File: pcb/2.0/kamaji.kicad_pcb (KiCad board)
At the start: 2 copper layers, 100 x 100 mm, 62 parts, among them J1 RJ10, J2 RJ10, J3 RJ10, J4 RJ10, J5 RJ10, J6 RJ10, J7 USB_B, J8 USB_A, Q1 2N3904, Q2 IRL540N, Q3 IRL540N, SW1 SW_Push, SW2 SW_Push, SW3 SW_Push, U1 ATMEGA32U4-AU, Y1 16MHz

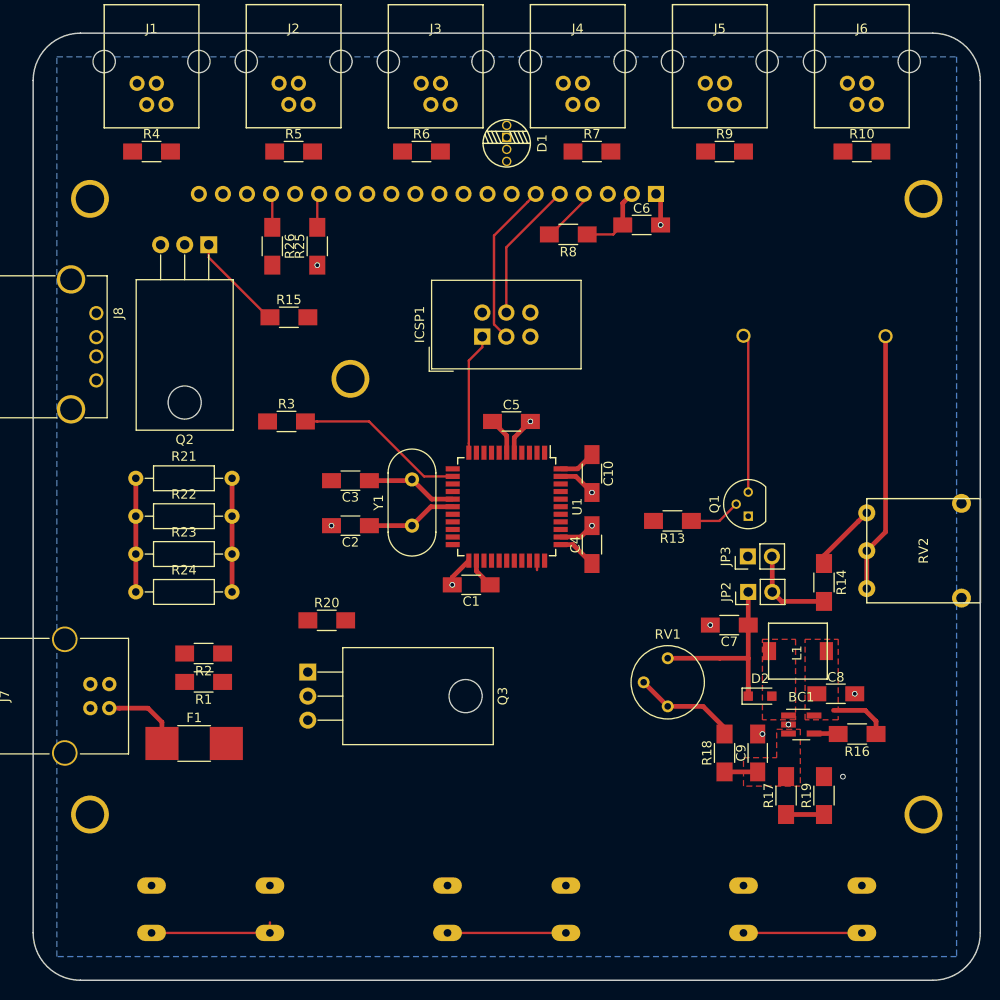
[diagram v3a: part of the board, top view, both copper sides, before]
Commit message: first attempt at laying out the 2.0 pcb
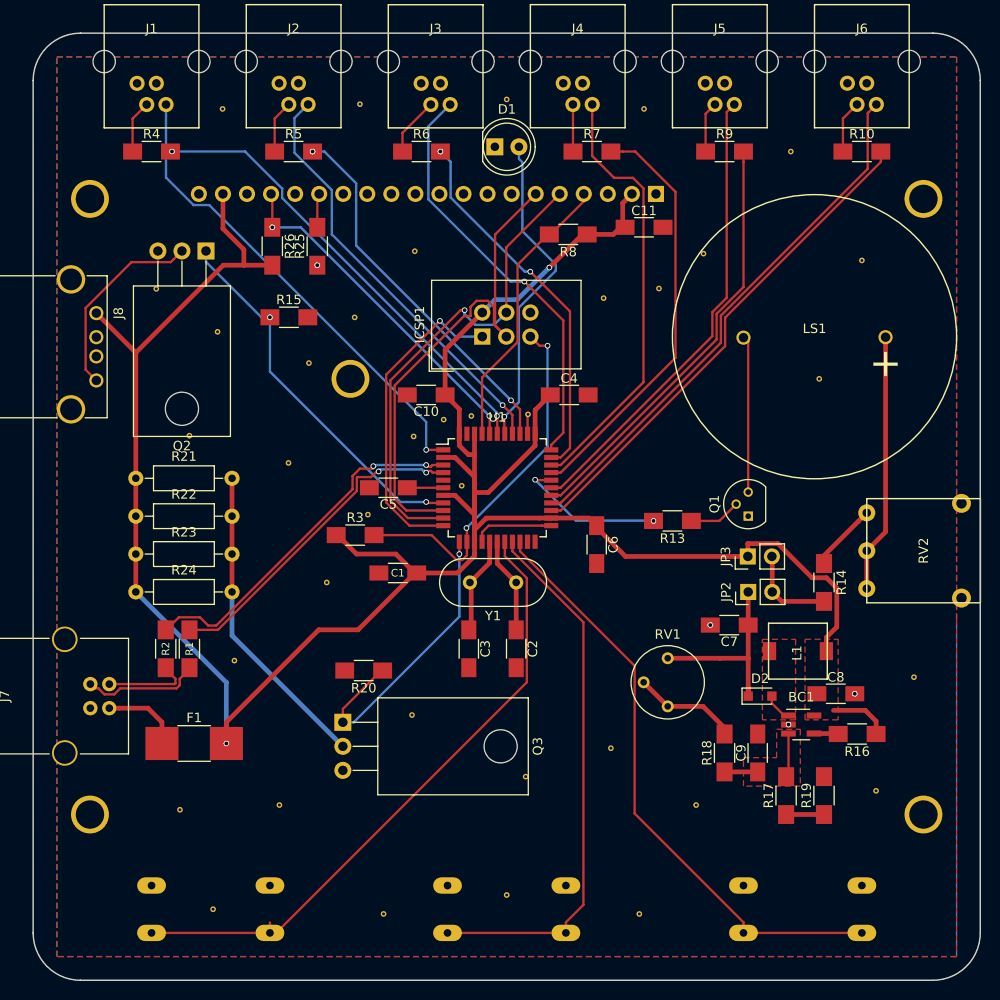
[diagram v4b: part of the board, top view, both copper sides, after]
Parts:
- added C11: 0.1uF, Capacitors_SMD:C_1206_HandSoldering, F.Cu at (114.5, 70.5)
- added REF**: Via_0.6mm, kamaji:Via_0.6mm, F.Cu at (102.2, 90.2)
- added REF**: Via_0.6mm, kamaji:Via_0.6mm, F.Cu at (71.2, 116.2)
- added REF**: Via_0.6mm, kamaji:Via_0.6mm, F.Cu at (81.0, 108.0)
- added REF**: Via_0.6mm, kamaji:Via_0.6mm, F.Cu at (90.0, 122.0)
- added REF**: Via_0.6mm, kamaji:Via_0.6mm, F.Cu at (65.5, 132.0)
- added REF**: Via_0.6mm, kamaji:Via_0.6mm, F.Cu at (69.0, 142.5)
- added REF**: Via_0.6mm, kamaji:Via_0.6mm, F.Cu at (76.0, 131.5)
- added REF**: Via_0.6mm, kamaji:Via_0.6mm, F.Cu at (87.0, 143.0)
- added REF**: Via_0.6mm, kamaji:Via_0.6mm, F.Cu at (100.0, 141.0)
- added REF**: Via_0.6mm, kamaji:Via_0.6mm, F.Cu at (102.0, 128.5)
- added REF**: Via_0.6mm, kamaji:Via_0.6mm, F.Cu at (111.0, 125.5)
- added REF**: Via_0.6mm, kamaji:Via_0.6mm, F.Cu at (63.0, 77.0)
- added REF**: Via_0.6mm, kamaji:Via_0.6mm, F.Cu at (114.0, 143.0)
- added REF**: Via_0.6mm, kamaji:Via_0.6mm, F.Cu at (120.0, 131.5)
- added REF**: Via_0.6mm, kamaji:Via_0.6mm, F.Cu at (143.0, 118.0)
- added REF**: Via_0.6mm, kamaji:Via_0.6mm, F.Cu at (139.0, 130.0)
- added REF**: Via_0.6mm, kamaji:Via_0.6mm, F.Cu at (120.8, 73.3)
- added REF**: Via_0.6mm, kamaji:Via_0.6mm, F.Cu at (116.1, 77.0)
- added REF**: Via_0.6mm, kamaji:Via_0.6mm, F.Cu at (110.2, 78.0)
- added REF**: Via_0.6mm, kamaji:Via_0.6mm, F.Cu at (90.3, 73.0)
- added REF**: Via_0.6mm, kamaji:Via_0.6mm, F.Cu at (83.9, 80.0)
- added REF**: Via_0.6mm, kamaji:Via_0.6mm, F.Cu at (79.1, 84.8)
- added REF**: Via_0.6mm, kamaji:Via_0.6mm, F.Cu at (70.0, 58.0)
- added REF**: Via_0.6mm, kamaji:Via_0.6mm, F.Cu at (69.5, 81.5)
- added REF**: Via_0.6mm, kamaji:Via_0.6mm, F.Cu at (66.5, 92.5)
- added REF**: Via_0.6mm, kamaji:Via_0.6mm, F.Cu at (77.0, 95.4)
- added REF**: Via_0.6mm, kamaji:Via_0.6mm, F.Cu at (85.3, 100.8)
- added REF**: Via_0.6mm, kamaji:Via_0.6mm, F.Cu at (90.2, 92.6)
- added REF**: Via_0.6mm, kamaji:Via_0.6mm, F.Cu at (93.3, 90.8)
- added REF**: Via_0.6mm, kamaji:Via_0.6mm, F.Cu at (96.3, 90.4)
- added REF**: Via_0.6mm, kamaji:Via_0.6mm, F.Cu at (95.2, 97.8)
- added REF**: Via_0.6mm, kamaji:Via_0.6mm, F.Cu at (84.5, 57.5)
- added REF**: Via_0.6mm, kamaji:Via_0.6mm, F.Cu at (100.0, 57.0)
- added REF**: Via_0.6mm, kamaji:Via_0.6mm, F.Cu at (114.5, 58.0)
- added REF**: Via_0.6mm, kamaji:Via_0.6mm, F.Cu at (130.0, 62.5)
- added REF**: Via_0.6mm, kamaji:Via_0.6mm, F.Cu at (137.5, 74.0)
- added REF**: Via_0.6mm, kamaji:Via_0.6mm, F.Cu at (133.0, 86.5)
- C1: value 0.1uF -> 10uF
- D1: value LED_CRGB -> LED; footprint kamaji:LED_RGB_common_cathode_5mm -> LEDs:LED_D5.0mm
- LS1: moved to F.Cu
- moved C6 34.1 mm to (109.5, 104.0), turned to 270 degrees
- moved C2 21.8 mm to (101.0, 115.0), turned to 270 degrees
- moved C3 21.7 mm to (96.0, 115.0), turned to 270 degrees
- moved C10 19.4 mm to (91.5, 88.2), turned to 180 degrees
- moved C4 16.0 mm to (106.6, 88.2), turned to 0 degrees
- moved C5 14.8 mm to (87.5, 98.0), turned to 180 degrees
- moved R3 14.0 mm to (84.0, 103.0)
- moved Y1 12.5 mm to (101.0, 108.0), turned to 180 degrees
- moved C1 7.85 mm to (88.5, 107.0)
- moved R20 6.58 mm to (84.9, 117.3), turned to 180 degrees
- moved Q3 6.46 mm to (82.7, 122.8)
- moved R2 4.03 mm to (64.0, 115.0), turned to 270 degrees
- moved R1 3.81 mm to (66.5, 115.0), turned to 270 degrees
- moved U1 2.24 mm to (99.0, 98.0), turned to 0 degrees
- moved D1 1.30 mm to (98.8, 62.0), turned to 0 degrees
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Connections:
- net /SIGNAL_R renamed /SIGNAL_LED
- J7 pad 2: /USB_D- -> /USBBD-
- J7 pad 3: /USB_D+ -> /USBBD+
- R1 pad 1: Net-(R1-Pad1) -> /USB_D+
- R1 pad 2: /USB_D+ -> /USBBD+
- R2 pad 1: Net-(R2-Pad1) -> /USB_D-
- R2 pad 2: /USB_D- -> /USBBD-
- U1 pad 1: /CBTN3 -> /PBTN1
- U1 pad 18: /PBTN1 -> /CBTN1
- U1 pad 19: /PLED1 -> /CBTN2
- U1 pad 20: /PBTN2 -> /CBTN3
- U1 pad 21: /PLED2 -> (no net)
- U1 pad 22: /PLED6 -> (no net)
- U1 pad 25: /PLED3 -> /PLED6
- U1 pad 26: /PBTN3 -> /PBTN6
- U1 pad 27: /PLED4 -> /PLED5
- U1 pad 28: /PBTN4 -> /PBTN5
- U1 pad 3: Net-(R2-Pad1) -> /USB_D-
- U1 pad 30: /PLED5 -> /PLED4
- U1 pad 31: /PBTN5 -> /PBTN4
- U1 pad 32: /CBTN1 -> /PLED3
- U1 pad 33: /CBTN2 -> /PBTN3
- U1 pad 36: /SIGNAL_B -> /PLED2
- U1 pad 37: /SIGNAL_G -> /PBTN2
- U1 pad 39: /PBTN6 -> /PLED1
- U1 pad 4: Net-(R1-Pad1) -> /USB_D+
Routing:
- net VCC: track 37.5 -> 266.9 mm, vias 0 -> 2
- net /PBTN6: track 0.00 -> 56.9 mm
- net /PLED6: track 0.00 -> 52.9 mm
- net /CBTN1: track 14.6 -> 67.5 mm
- net /CBTN3: track 12.5 -> 63.6 mm
- net /PBTN1: track 0.00 -> 50.6 mm, vias 0 -> 1
- net /PBTN5: track 0.00 -> 49.1 mm
- net /PLED1: track 0.00 -> 48.6 mm, vias 0 -> 2
- net /PBTN4: track 0.00 -> 46.1 mm
- net /PLED5: track 0.00 -> 45.3 mm
- net /CBTN2: track 13.2 -> 58.3 mm
- net /PBTN2: track 0.00 -> 44.9 mm, vias 0 -> 1
- net /PBTN3: track 0.00 -> 44.7 mm, vias 0 -> 1
- net /PLED4: track 0.00 -> 44.3 mm
- net /PLED3: track 0.00 -> 39.7 mm, vias 0 -> 2
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- added copper zone on F.Cu, net GND
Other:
- net class Default: clearance 0.2 -> 0.1524
- net class Power: clearance 0.25 -> 0.254
- rule trace_clearance: 0.2 -> 0.1524

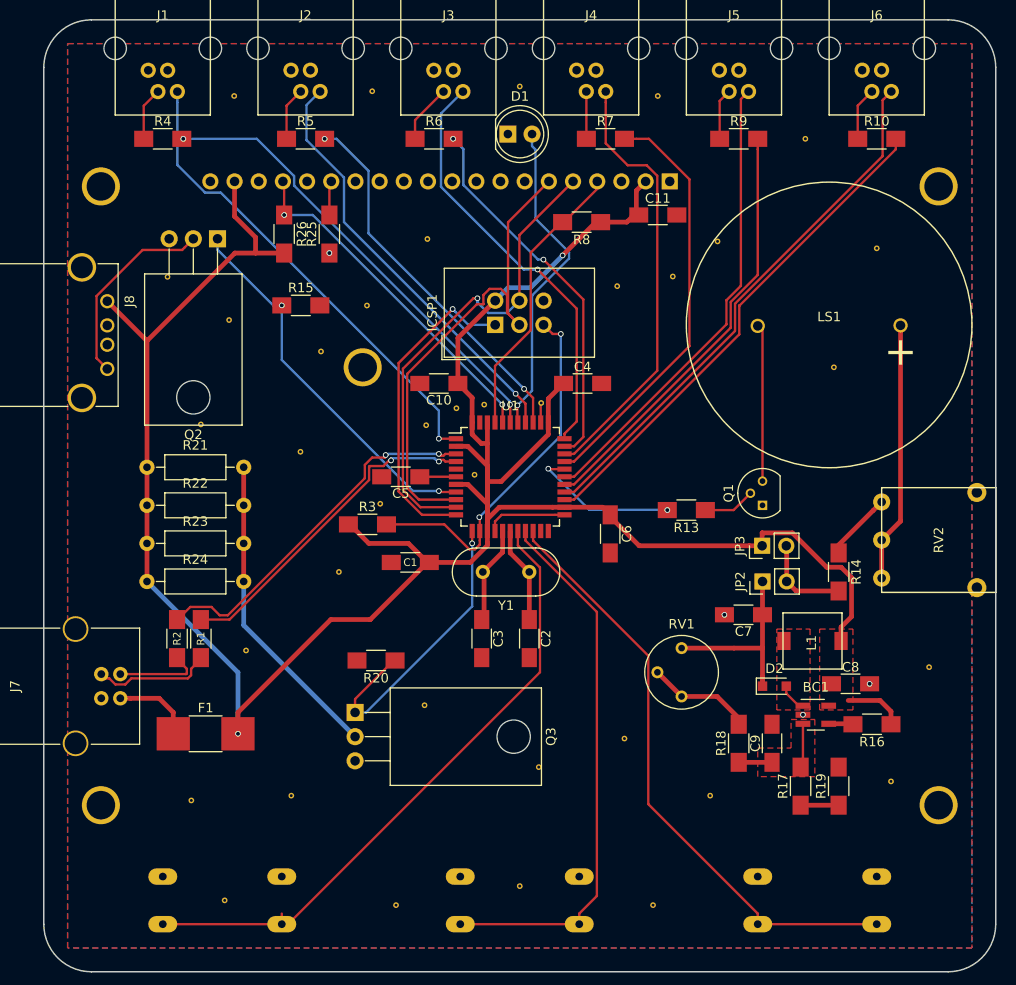
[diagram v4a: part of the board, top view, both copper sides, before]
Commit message: add stitching vias, mounting holes
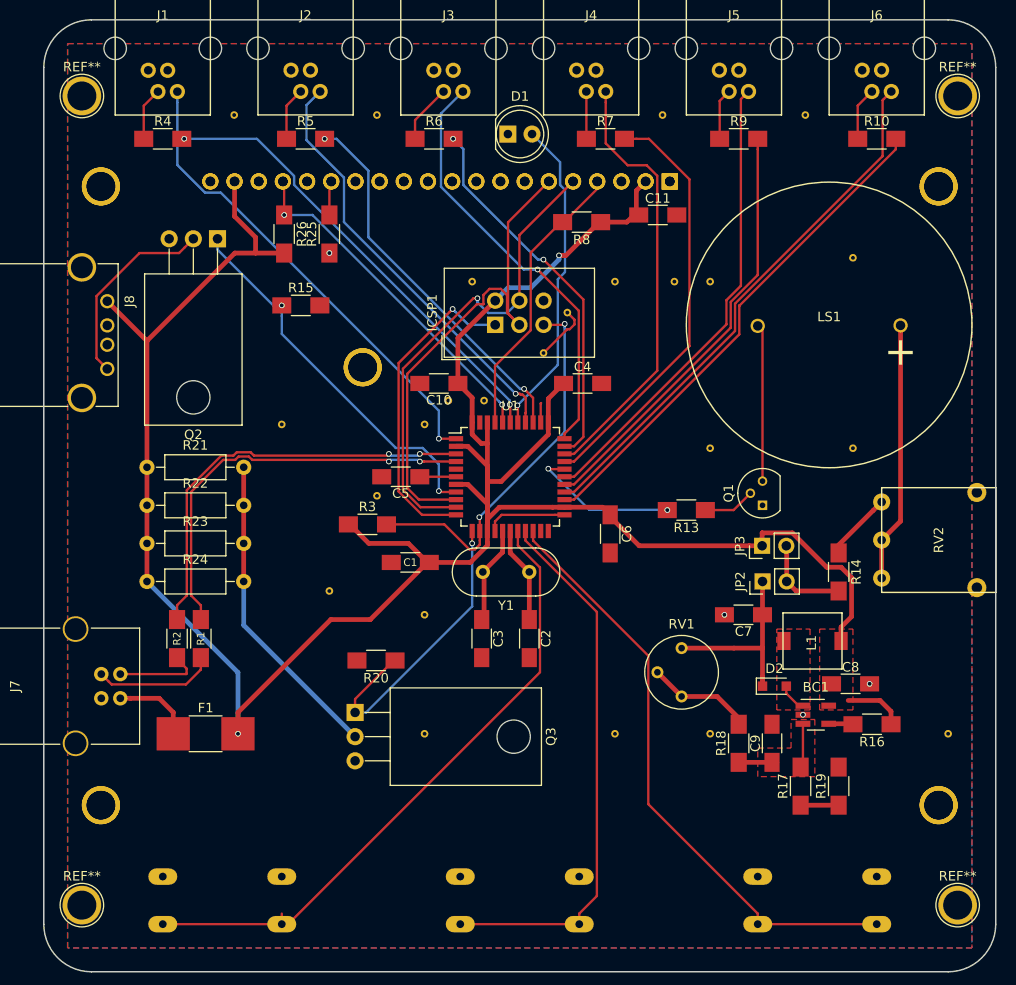
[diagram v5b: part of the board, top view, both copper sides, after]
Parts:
- removed the REF** at (102.2, 90.2)
- removed the REF** at (71.2, 116.2)
- removed the REF** at (81.0, 108.0)
- removed the REF** at (90.0, 122.0)
- removed the REF** at (65.5, 132.0)
- removed the REF** at (69.0, 142.5)
- removed the REF** at (76.0, 131.5)
- removed the REF** at (87.0, 143.0)
- removed the REF** at (100.0, 141.0)
- removed the REF** at (102.0, 128.5)
- removed the REF** at (111.0, 125.5)
- removed the REF** at (63.0, 77.0)
- removed the REF** at (114.0, 143.0)
- removed the REF** at (120.0, 131.5)
- removed the REF** at (143.0, 118.0)
- removed the REF** at (139.0, 130.0)
- removed the REF** at (120.8, 73.3)
- removed the REF** at (116.1, 77.0)
- removed the REF** at (110.2, 78.0)
- removed the REF** at (90.3, 73.0)
- removed the REF** at (83.9, 80.0)
- removed the REF** at (79.1, 84.8)
- removed the REF** at (70.0, 58.0)
- removed the REF** at (69.5, 81.5)
- removed the REF** at (66.5, 92.5)
- removed the REF** at (77.0, 95.4)
- removed the REF** at (85.3, 100.8)
- removed the REF** at (90.2, 92.6)
- removed the REF** at (93.3, 90.8)
- removed the REF** at (96.3, 90.4)
- removed the REF** at (95.2, 97.8)
- removed the REF** at (84.5, 57.5)
- removed the REF** at (100.0, 57.0)
- removed the REF** at (114.5, 58.0)
- removed the REF** at (130.0, 62.5)
- removed the REF** at (137.5, 74.0)
- removed the REF** at (133.0, 86.5)
- added DS1: LCD12864B, kamaji:LCD12864, B.Cu at (100.0, 100.0)
- added REF**: 1pin, Connectors:1pin, F.Cu at (146.0, 143.0)
- added REF**: 1pin, Connectors:1pin, F.Cu at (54.0, 143.0)
- added REF**: 1pin, Connectors:1pin, F.Cu at (146.0, 58.0)
- added REF**: 1pin, Connectors:1pin, F.Cu at (54.0, 58.0)
- added VIA**: Via_0.8mm, kamaji:Via_0.8mm, F.Cu at (105.0, 80.8)
- added VIA**: Via_0.8mm, kamaji:Via_0.8mm, F.Cu at (130.0, 60.0)
- added VIA**: Via_0.8mm, kamaji:Via_0.8mm, F.Cu at (135.0, 75.0)
- added VIA**: Via_0.8mm, kamaji:Via_0.8mm, F.Cu at (135.0, 95.0)
- added VIA**: Via_0.8mm, kamaji:Via_0.8mm, F.Cu at (120.0, 95.0)
- added VIA**: Via_0.8mm, kamaji:Via_0.8mm, F.Cu at (116.2, 77.5)
- added VIA**: Via_0.8mm, kamaji:Via_0.8mm, F.Cu at (120.0, 77.5)
- added VIA**: Via_0.8mm, kamaji:Via_0.8mm, F.Cu at (110.0, 77.5)
- added VIA**: Via_0.8mm, kamaji:Via_0.8mm, F.Cu at (96.2, 90.0)
- added VIA**: Via_0.8mm, kamaji:Via_0.8mm, F.Cu at (102.5, 85.0)
- added VIA**: Via_0.8mm, kamaji:Via_0.8mm, F.Cu at (80.0, 110.0)
- added VIA**: Via_0.8mm, kamaji:Via_0.8mm, F.Cu at (145.0, 125.0)
- added VIA**: Via_0.8mm, kamaji:Via_0.8mm, F.Cu at (90.0, 112.5)
- added VIA**: Via_0.8mm, kamaji:Via_0.8mm, F.Cu at (85.0, 100.0)
- added VIA**: Via_0.8mm, kamaji:Via_0.8mm, F.Cu at (92.5, 90.0)
- added VIA**: Via_0.8mm, kamaji:Via_0.8mm, F.Cu at (90.0, 92.5)
- added VIA**: Via_0.8mm, kamaji:Via_0.8mm, F.Cu at (75.0, 92.5)
- added VIA**: Via_0.8mm, kamaji:Via_0.8mm, F.Cu at (120.0, 125.0)
- added VIA**: Via_0.8mm, kamaji:Via_0.8mm, F.Cu at (110.0, 125.0)
- added VIA**: Via_0.8mm, kamaji:Via_0.8mm, F.Cu at (90.0, 125.0)
- added VIA**: Via_0.8mm, kamaji:Via_0.8mm, F.Cu at (70.0, 60.0)
- added VIA**: Via_0.8mm, kamaji:Via_0.8mm, F.Cu at (85.0, 60.0)
- added VIA**: Via_0.8mm, kamaji:Via_0.8mm, F.Cu at (95.0, 77.5)
- added VIA**: Via_0.8mm, kamaji:Via_0.8mm, F.Cu at (115.0, 60.0)
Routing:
- net /USB_D+: track 35.1 -> 43.6 mm
- net /USB_D-: track 38.4 -> 45.0 mm
- net GND: track 11.4 -> 17.4 mm
- net /RST: track 39.0 -> 40.3 mm
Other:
- net class Default: clearance 0.1524 -> 0.2
- net class Power: clearance 0.254 -> 0.2
- rule trace_clearance: 0.1524 -> 0.2
